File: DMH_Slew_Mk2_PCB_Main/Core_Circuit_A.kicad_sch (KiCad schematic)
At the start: 60 parts, among them J1 TS_Jack_6.35mm_Sw, J11 Conn_02x03_Top_Bottom, J12 Conn_02x06_Top_Bottom, J13 Conn_02x03_Top_Bottom, J14 Conn_02x03_Top_Bottom, J15 Conn_02x06_Top_Bottom, J16 Conn_02x03_Top_Bottom, J17 Conn_01x08, J18 Conn_01x08, J19 Conn_01x08, J2 TS_Jack_6.35mm_Sw, J20 Conn_01x08, J3 TS_Jack_6.35mm_Sw, Q1 BC548, Q2 BC548, Q3 BC558, Q4 BC558, SW1 SW_DPDT_3way, SW2 SW_DPDT, SW3 SPDT_OnOffOn, U1 TL074, U2 TL074

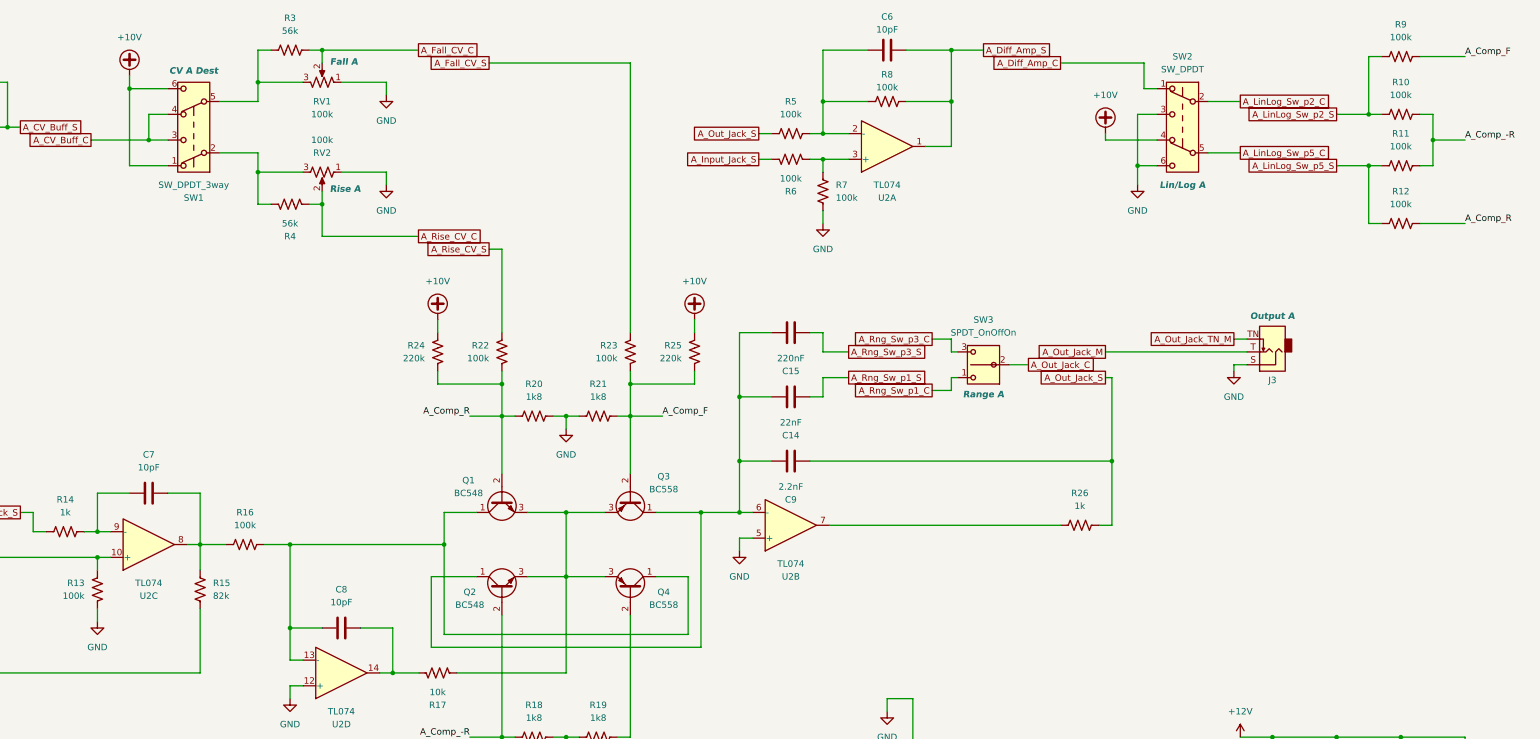
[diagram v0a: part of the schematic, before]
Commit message: Redesigned panel and main PCB schematic
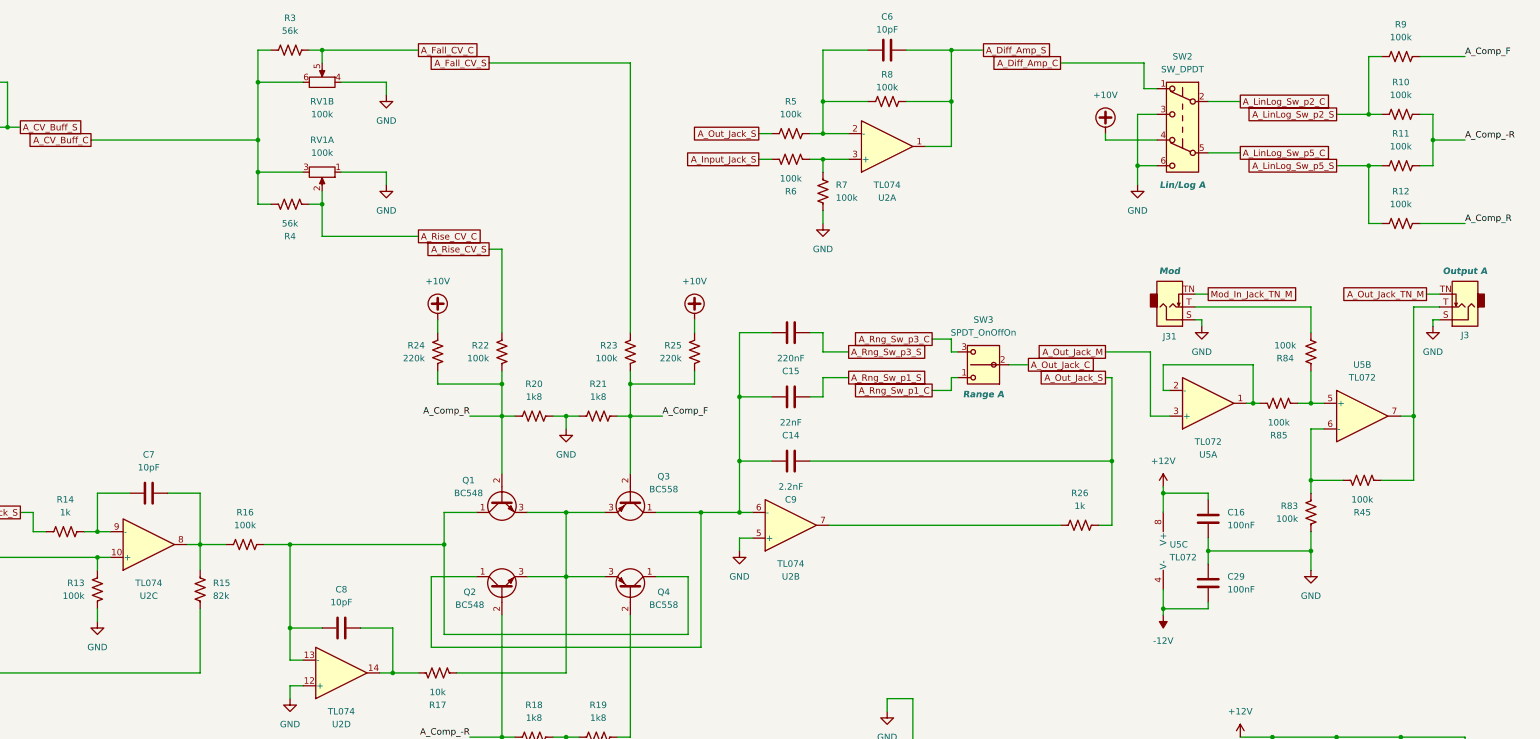
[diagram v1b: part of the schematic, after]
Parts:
- removed RV1, RV2: 100k, SynthStuff:Potentiometer_Alpha_RD901F-40-00D_Single_Vertical, symbol Device:R_Potentiometer_US
- removed SW1: SW_DPDT_3way, SynthStuff:Toggle_Switch_2_Poles_TE, symbol SynthStuff:Switch_DPDT
- added C16, C29: 100nF, Capacitor_THT:C_Disc_D4.3mm_W1.9mm_P5.00mm, symbol Device:C
- added J31: TS_Jack_6.35mm_Sw, SynthStuff:CUI_MJ-63052A, symbol SynthStuff:TS_Jack_6.35mm_Sw
- added R45, R83, R84, R85: 100k, Resistor_THT:R_Axial_DIN0207_L6.3mm_D2.5mm_P7.62mm_Horizontal, symbol Device:R_US
- added RV1: 100k, Potentiometer_THT:Potentiometer_Alpha_RD902F-40-00D_Dual_Vertical, symbol Device:R_Potentiometer_Dual_Separate
- added U5: TL072, Package_DIP:DIP-8_W7.62mm_Socket, symbol Amplifier_Operational:TL072
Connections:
- net +12V: now also C16.1, U5.8 (V+)
- net -12V: now also C29.2, U5.4 (V-)
- net A_CV_Buff_C: now also R3.2, R4.2, RV1.3, RV1.6
- net A_Fall_CV_C: now also RV1.5
- net A_Out_Jack_M: now also U5.3 (+); no longer J3.T
- net A_Rise_CV_C: now also RV1.2
- net GND: now also C16.2, C29.1, J31.S, R83.2, RV1.1, RV1.4
- new net: J31.T, R84.1
- new net: R84.2, R85.1, U5.5 (+)
- new net: R85.2, U5.1, U5.2 (-)
- new net: J3.T, R45.1, U5.7
- new net: R45.2, R83.1, U5.6 (-)
- new net Mod_In_Jack_TN_M: J31.TN
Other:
- moved on the sheet: J3
